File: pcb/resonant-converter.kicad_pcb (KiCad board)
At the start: 4 copper layers, 100 x 100 mm, 33 parts, among them J1 Banana_Jack_Keystone_575-8, J2 Banana_Jack_Keystone_575-8, J3 Banana_Jack_Keystone_575-8, J4 Banana_Jack_Keystone_575-8, Q1 SIS472DN-T1-GE3, Q2 SIS472DN-T1-GE3, Q3 SIS472DN-T1-GE3, Q4 SIS472DN-T1-GE3, T1 B66206W1110T001, U1 UCC256610DDBR, U2 TEA2096T/1J, U3 INA219BIDCNR, U4 PC817X2CSP9F, U5 TL431AIDBVR

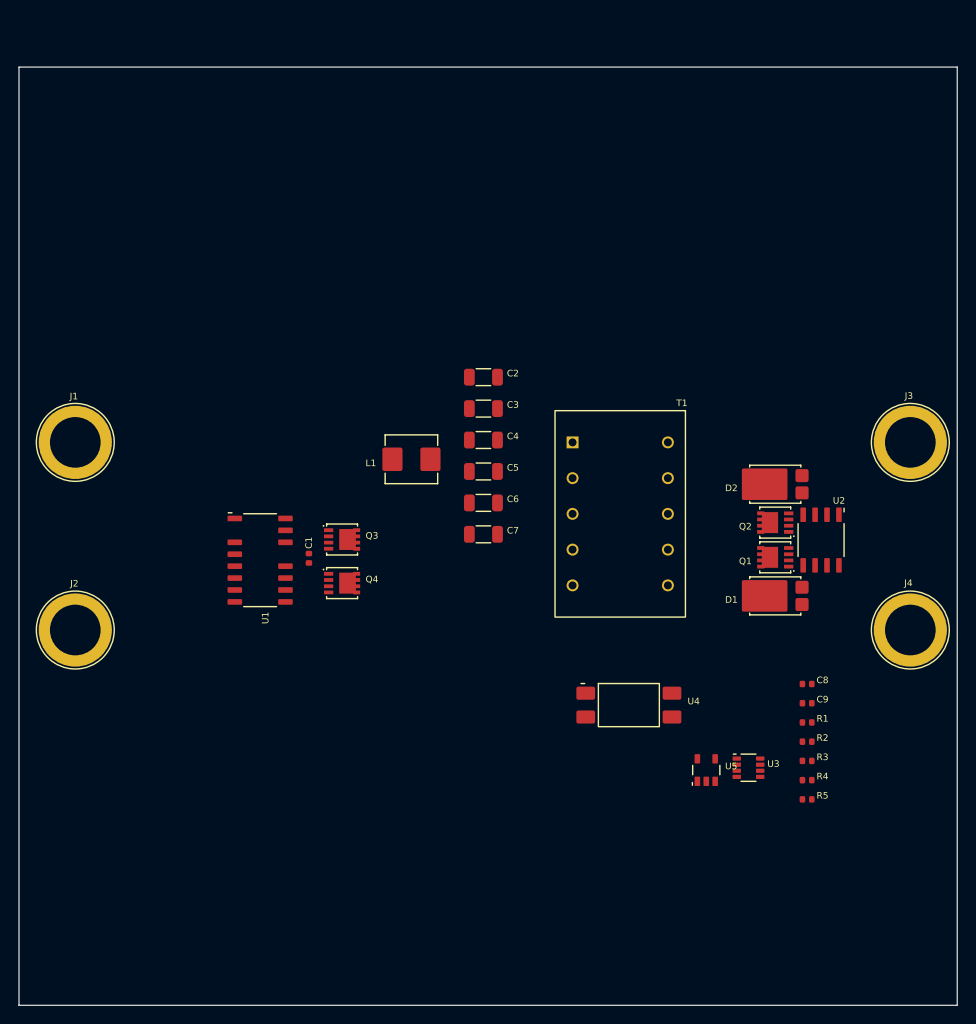
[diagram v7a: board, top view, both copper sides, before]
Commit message: Update PCB from schematic, add project info block on silkscreen
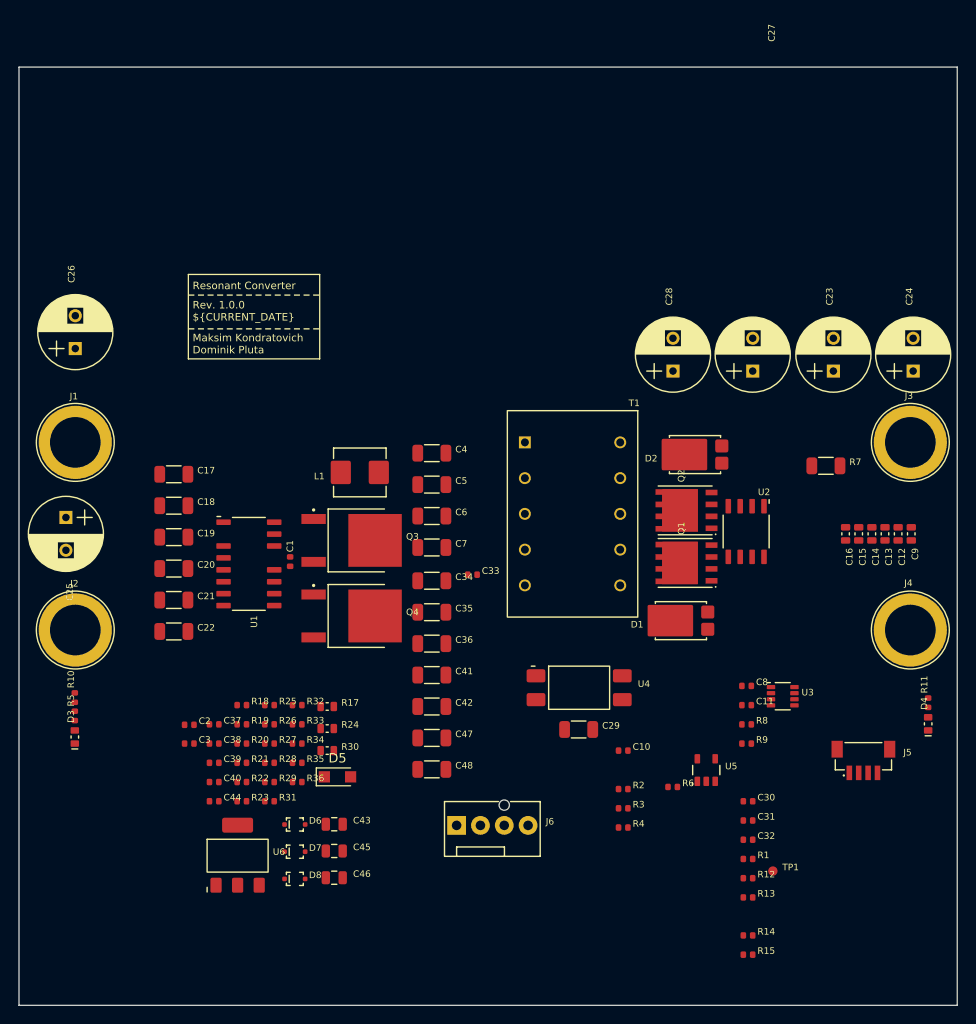
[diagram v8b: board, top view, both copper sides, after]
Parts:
- added C10: C-1n-0402, DW-footprints:C_0402_1005Metric, F.Cu at (164.4, 122.8)
- added C11: C-1u-0402, DW-footprints:C_0402_1005Metric, F.Cu at (177.6, 118.0)
- added C12: C-10u-0603, DW-footprints:C_0603_1608Metric, F.Cu at (193.7, 99.8)
- added C13: C-10u-0603, DW-footprints:C_0603_1608Metric, F.Cu at (192.3, 99.8)
- added C14: C-10u-0603, DW-footprints:C_0603_1608Metric, F.Cu at (190.9, 99.8)
- added C15: C-10u-0603, DW-footprints:C_0603_1608Metric, F.Cu at (189.5, 99.8)
- added C16: C-10u-0603, DW-footprints:C_0603_1608Metric, F.Cu at (188.1, 99.8)
- added C17: C-2u2-100V-1206, DW-footprints:C_1206_3216Metric, F.Cu at (116.5, 93.4)
- added C18: C-2u2-100V-1206, DW-footprints:C_1206_3216Metric, F.Cu at (116.5, 96.8)
- added C19: C-2u2-100V-1206, DW-footprints:C_1206_3216Metric, F.Cu at (116.5, 100.1)
- added C20: C-2u2-100V-1206, DW-footprints:C_1206_3216Metric, F.Cu at (116.5, 103.5)
- added C21: C-2u2-100V-1206, DW-footprints:C_1206_3216Metric, F.Cu at (116.5, 106.8)
- added C22: C-2u2-100V-1206, DW-footprints:C_1206_3216Metric, F.Cu at (116.5, 110.2)
- added C23: C_Pol_47u_100V_D8mm_H11.5, DW-footprints:C_Pol_D8mm_H11.5mm_P3.5mm, F.Cu at (186.8, 82.4)
- added C24: C_Pol_47u_100V_D8mm_H11.5, DW-footprints:C_Pol_D8mm_H11.5mm_P3.5mm, F.Cu at (195.3, 82.4)
- added C25: C_Pol_47u_100V_D8mm_H11.5, DW-footprints:C_Pol_D8mm_H11.5mm_P3.5mm, F.Cu at (105.0, 98.0)
- added C26: C_Pol_47u_100V_D8mm_H11.5, DW-footprints:C_Pol_D8mm_H11.5mm_P3.5mm, F.Cu at (106.0, 80.0)
- added C27: C_Pol_47u_100V_D8mm_H11.5, DW-footprints:C_Pol_D8mm_H11.5mm_P3.5mm, F.Cu at (178.2, 82.4)
- added C28: C_Pol_47u_100V_D8mm_H11.5, DW-footprints:C_Pol_D8mm_H11.5mm_P3.5mm, F.Cu at (169.7, 82.4)
- added C29: C-1n-2kV-1206, DW-footprints:C_1206_3216Metric, F.Cu at (159.7, 120.6)
- added C30: C-100p-0402, DW-footprints:C_0402_1005Metric, F.Cu at (177.7, 128.2)
- added C31: C-1u-0402, DW-footprints:C_0402_1005Metric, F.Cu at (177.7, 130.3)
- added C32: C-100p-0402, DW-footprints:C_0402_1005Metric, F.Cu at (177.7, 132.3)
- added C33: 4.7n, DW-footprints:C_0402_1005Metric, F.Cu at (148.3, 104.1)
- added C34: C-10n-100V-C0G-1206, DW-footprints:C_1206_3216Metric, F.Cu at (144.0, 104.8)
- added C35: C-10n-100V-C0G-1206, DW-footprints:C_1206_3216Metric, F.Cu at (144.0, 108.1)
- added C36: C-10n-100V-C0G-1206, DW-footprints:C_1206_3216Metric, F.Cu at (144.0, 111.5)
- added C37: C-1u-0402, DW-footprints:C_0402_1005Metric, F.Cu at (120.8, 120.0)
- added C38: C-1u-0402, DW-footprints:C_0402_1005Metric, F.Cu at (120.8, 122.1)
- added C39: C-150p-0402, DW-footprints:C_0402_1005Metric, F.Cu at (120.8, 124.2)
- added C40: C-1n-0402, DW-footprints:C_0402_1005Metric, F.Cu at (120.8, 126.2)
- added C41: C-22n-100V-C0G-1206, DW-footprints:C_1206_3216Metric, F.Cu at (144.0, 114.8)
- added C42: C-22n-100V-C0G-1206, DW-footprints:C_1206_3216Metric, F.Cu at (144.0, 118.2)
- added C43: C-10u-0805, DW-footprints:C_0805_2012Metric, F.Cu at (133.6, 130.7)
- added C44: C-100p-0402, DW-footprints:C_0402_1005Metric, F.Cu at (120.8, 128.2)
- added C45: C-10u-0805, DW-footprints:C_0805_2012Metric, F.Cu at (133.6, 133.6)
- added C46: C-10u-0805, DW-footprints:C_0805_2012Metric, F.Cu at (133.6, 136.4)
- added C47: C-10n-100V-C0G-1206, DW-footprints:C_1206_3216Metric, F.Cu at (144.0, 121.5)
- added C48: C-10n-100V-C0G-1206, DW-footprints:C_1206_3216Metric, F.Cu at (144.0, 124.8)
- added D3: LED-R-0603_KT-0603R, DW-footprints:LED_0603_1608Metric_R, F.Cu at (106.0, 121.4)
- added D4: LED-R-0603_KT-0603R, DW-footprints:LED_0603_1608Metric_R, F.Cu at (196.9, 120.0)
- added D5: PMEG10020AELR, Diode_SMD:Nexperia_CFP3_SOD-123W, F.Cu at (133.9, 125.7)
- added D6: 1N4148WS-AU, DW-footprints:D_SOD-323F, F.Cu at (129.4, 130.7)
- added D7: 1N4148WS-AU, DW-footprints:D_SOD-323F, F.Cu at (129.4, 133.6)
- added D8: 1N4148WS-AU, DW-footprints:D_SOD-323F, F.Cu at (129.4, 136.5)
- added J5: JST_SH_1x4_BM04B-SRSS-TB-LF-SN, DW-footprints:Conn_JST_SH_1x4_BM04B-SRSS-TB, F.Cu at (190.0, 123.5)
- added J6: Molex_KK_1x4_0470531000, DW-footprints:Conn_Molex_KK_1x4_0470531000, F.Cu at (146.6, 130.8)
- added R10: R-10k-0402, DW-footprints:R_0402_1005Metric, F.Cu at (106.0, 117.2)
- added R11: R-10k-0402, DW-footprints:R_0402_1005Metric, F.Cu at (196.9, 117.8)
- added R12: R-0R-0402, DW-footprints:R_0402_1005Metric, F.Cu at (177.7, 136.4)
- added R13: R-10k-0402, DW-footprints:R_0402_1005Metric, F.Cu at (177.7, 138.5)
- added R14: R-10k-0402, DW-footprints:R_0402_1005Metric, F.Cu at (177.7, 142.6)
- added R15: R-10k-0402, DW-footprints:R_0402_1005Metric, F.Cu at (177.7, 144.6)
- added R17: R-1R-0603, DW-footprints:R_0603_1608Metric, F.Cu at (132.8, 118.2)
- added R18: R-10k-0402, DW-footprints:R_0402_1005Metric, F.Cu at (123.8, 118.0)
- added R19: R-100k-0402, DW-footprints:R_0402_1005Metric, F.Cu at (123.8, 120.0)
- added R20: R-100k-0402, DW-footprints:R_0402_1005Metric, F.Cu at (123.8, 122.1)
- added R21: R-33k-0402, DW-footprints:R_0402_1005Metric, F.Cu at (123.8, 124.2)
- added R22: R-4k7-0402, DW-footprints:R_0402_1005Metric, F.Cu at (123.8, 126.2)
- added R23: R-20k-0402, DW-footprints:R_0402_1005Metric, F.Cu at (123.8, 128.2)
- added R24: R-1R-0603, DW-footprints:R_0603_1608Metric, F.Cu at (132.8, 120.5)
- added R25: R-470R-0402, DW-footprints:R_0402_1005Metric, F.Cu at (126.7, 118.0)
- added R26: 430k, DW-footprints:R_0402_1005Metric, F.Cu at (126.7, 120.0)
- added R27: 120k, DW-footprints:R_0402_1005Metric, F.Cu at (126.7, 122.1)
- added R28: 510k, DW-footprints:R_0402_1005Metric, F.Cu at (126.7, 124.2)
- added R29: 430k, DW-footprints:R_0402_1005Metric, F.Cu at (126.7, 126.2)
- added R30: R-1R-0603, DW-footprints:R_0603_1608Metric, F.Cu at (132.8, 122.8)
- added R31: R-150R-0402, DW-footprints:R_0402_1005Metric, F.Cu at (126.7, 128.2)
- added R32: R-10k-0402, DW-footprints:R_0402_1005Metric, F.Cu at (129.7, 118.0)
- added R33: R-10k-0402, DW-footprints:R_0402_1005Metric, F.Cu at (129.7, 120.0)
- added R34: R-33R-0402, DW-footprints:R_0402_1005Metric, F.Cu at (129.7, 122.1)
- added R35: R-33R-0402, DW-footprints:R_0402_1005Metric, F.Cu at (129.7, 124.2)
- added R36: R-470R-0402, DW-footprints:R_0402_1005Metric, F.Cu at (129.7, 126.2)
- added R6: R-10k-0402, DW-footprints:R_0402_1005Metric, F.Cu at (169.7, 126.7)
- added R7: R-0R001-1206, DW-footprints:R_1206_3216Metric, F.Cu at (186.0, 92.5)
- added R8: R-22R-0402, DW-footprints:R_0402_1005Metric, F.Cu at (177.6, 120.1)
- added R9: R-22R-0402, DW-footprints:R_0402_1005Metric, F.Cu at (177.6, 122.1)
- added TP1: TP_SMD_1mm, DW-footprints:TP_SMD_1mm, F.Cu at (180.3, 135.7)
- added U6: 78L15MG, DW-footprints:SOT-223, F.Cu at (123.3, 134.1)
- C1: value C-1u-0402 -> C-1n-0402
- C2, C3: value C-22n-100V-C0G-1206 -> C-330p-0402; footprint DW-footprints:C_1206_3216Metric -> DW-footprints:C_0402_1005Metric
- C9: value C-22p-0402 -> C-10u-0603; footprint DW-footprints:C_0402_1005Metric -> DW-footprints:C_0603_1608Metric
- Q1, Q2: value SIS472DN-T1-GE3 -> MDU04N010VRH; footprint DW-footprints:PowerPAK-1212-8_Single -> DW-footprints:PDFN-56-8
- Q3, Q4: value SIS472DN-T1-GE3 -> HSU30N20; footprint DW-footprints:PowerPAK-1212-8_Single -> DW-footprints:TO-252-3
- R1, R2, R5: value R-1k-0402 -> R-10k-0402
- R3, R4: value R-1k-0402 -> R-39k-0402
- moved R5 78.6 mm to (106.0, 119.2), turned to 90 degrees
- moved C2 48.5 mm to (118.2, 120.1)
- moved C3 47.5 mm to (118.2, 122.1)
- moved C9 21.2 mm to (195.1, 99.8), turned to -90 degrees
- moved R4 20.2 mm to (164.4, 131.1)
- moved R2 20.2 mm to (164.4, 127.0)
- moved R3 20.2 mm to (164.4, 129.0)
- moved R1 15.9 mm to (177.7, 134.4)
- moved D1 10.4 mm to (170.6, 109.0)
- moved Q2 9.69 mm to (171.0, 97.2), turned to 90 degrees
- moved Q1 9.62 mm to (171.0, 102.8), turned to 90 degrees
- moved D2 9.12 mm to (172.1, 91.3)
- moved U3 8.45 mm to (181.4, 117.1)
- moved U2 8.04 mm to (177.5, 99.5)
- moved C8 6.45 mm to (177.6, 116.0)
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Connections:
- C1 pad 1: Net-(U1-HB) -> GND
- C1 pad 2: Net-(Q3-G) -> /BLK
- C2 pad 1: GNDPWR -> GND
- C2 pad 2: Net-(C2-Pad2) -> /LL
- C3 pad 1: GNDPWR -> GND
- C3 pad 2: Net-(C2-Pad2) -> /TSET
- C4 pad 1: GNDPWR -> GND
- C4 pad 2: Net-(C2-Pad2) -> /TRAFO_BOT
- C5 pad 1: GNDPWR -> GND
- C5 pad 2: Net-(C2-Pad2) -> /TRAFO_BOT
- C6 pad 1: GNDPWR -> GND
- C6 pad 2: Net-(C2-Pad2) -> /TRAFO_BOT
- C7 pad 1: GNDPWR -> GND
- C7 pad 2: Net-(C2-Pad2) -> /TRAFO_BOT
- C8 pad 1: GND -> GND_ISO
- C9 pad 1: Net-(U5-REF) -> GND_ISO
- C9 pad 2: Net-(C9-Pad2) -> +12V
- D1 pad 2: GND -> GND_ISO
- D2 pad 2: GND -> GND_ISO
- J1 pad 1: VCC -> +60V
- J2 pad 1: GNDPWR -> GND
- J4 pad 1: GND -> GND_ISO
- L1 pad 1: Net-(Q4-D) -> Net-(Q3-S)
- L1 pad 2: unconnected-(L1-Pad2) -> /TRAFO_TOP
- Q1 pad 1: GND -> GND_ISO
- Q1 pad 2: GND -> GND_ISO
- Q1 pad 3: GND -> GND_ISO
- Q2 pad 1: GND -> GND_ISO
- Q2 pad 2: GND -> GND_ISO
- Q2 pad 3: GND -> GND_ISO
- Q3 pad 1: Net-(Q4-D) -> Net-(Q3-G)
- Q3 pad 2: Net-(Q4-D) -> Net-(Q3-S)
- Q3 pad 3: Net-(Q4-D) -> +60V
- Q4 pad 1: GNDPWR -> Net-(Q4-G)
- Q4 pad 2: GNDPWR -> GND
- Q4 pad 3: GNDPWR -> Net-(Q3-S)
- R1 pad 1: Net-(U5-K) -> Net-(R1-Pad1)
- R1 pad 2: Net-(R1-Pad2) -> Net-(C31-Pad2)
- R2 pad 1: Net-(R1-Pad2) -> Net-(U5-K)
- R2 pad 2: +12V -> Net-(R1-Pad1)
- R3 pad 1: GND -> /V_FB
- R3 pad 2: Net-(U5-REF) -> +12V
- R4 pad 1: Net-(U5-REF) -> Net-(U5-K)
- R4 pad 2: +12V -> Net-(C10-Pad1)
- R5 pad 1: Net-(C9-Pad2) -> Net-(D3-A)
- R5 pad 2: Net-(U5-K) -> Net-(R10-Pad1)
- T1 pad 1: unconnected-(T1-Pad1) -> /TRAFO_TOP
- T1 pad 3: unconnected-(T1-Pad3) -> /TRAFO_BOT
- T1 pad 4: unconnected-(T1-Pad4) -> /TRAFO_AUX
- T1 pad 5: unconnected-(T1-Pad5) -> GND
- T1 pad 8: +12V -> /+12V_R
- T1 pad 9: +12V -> /+12V_R
- U1 pad 1: unconnected-(U1-HV-Pad1) -> /HV
- U1 pad 10: GNDPWR -> GND
- U1 pad 11: Net-(Q4-G) -> Net-(D8-C)
- U1 pad 12: unconnected-(U1-VCCP-Pad12) -> VCCP
- U1 pad 15: Net-(Q3-G) -> Net-(D6-C)
- U1 pad 16: Net-(Q4-D) -> Net-(Q3-S)
- U1 pad 3: unconnected-(U1-BLK-Pad3) -> /BLK
- U1 pad 4: unconnected-(U1-OVP/OTP-Pad4) -> /OVP/OTP
- U1 pad 5: unconnected-(U1-FB-Pad5) -> /FB
- U1 pad 6: unconnected-(U1-LL-Pad6) -> /LL
- U1 pad 7: unconnected-(U1-TSET-Pad7) -> /TSET
- U1 pad 8: unconnected-(U1-V5P-Pad8) -> /V5P
- U1 pad 9: unconnected-(U1-ISNS-Pad9) -> /ISNS
- U2 pad 2: GND -> GND_ISO
- U2 pad 4: GND -> GND_ISO
- U2 pad 5: GND -> GND_ISO
- U2 pad 7: +12V -> /+12V_R
- U3 pad 1: unconnected-(U3-IN+-Pad1) -> Net-(U3-IN+)
- U3 pad 2: unconnected-(U3-IN--Pad2) -> Net-(U3-IN-)
- U3 pad 3: GND -> GND_ISO
- U3 pad 5: unconnected-(U3-SCL-Pad5) -> /Power monitor/SCL
- U3 pad 6: unconnected-(U3-SDA-Pad6) -> /Power monitor/SDA
- U3 pad 7: GND -> GND_ISO
- U3 pad 8: GND -> GND_ISO
- U4 pad 1: Net-(R1-Pad2) -> Net-(R1-Pad1)
- U4 pad 3: unconnected-(U4-Pad3) -> Net-(R18-Pad2)
- U4 pad 4: unconnected-(U4-Pad4) -> /FB
- U5 pad 4: Net-(U5-REF) -> /V_FB
- U5 pad 5: GND -> GND_ISO
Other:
- board text added: "Maksim Kondratovich Dominik Pluta"
- board text added: "Resonant Converter"
- board text added: "Rev. ${REVISION} ${CURRENT_DATE}"
- board text added: "SHA: %%%%%%%%"
